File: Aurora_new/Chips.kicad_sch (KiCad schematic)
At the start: 84 parts, among them J1 UJ20-C-H-C-3-SMT-TR, J16 PPPC042LFBN-RC, J3 PPPC042LFBN-RC, J36 PPPC042LFBN-RC, J41 STEMMA QT, J6 DM3AT-SF-PEJM5, U1 STM32H757BITx, U13 XBP9X-DMUS-001, U14 MS5611-01BA, U2 USBLC6-2SC6, U3 TPS2121RUXR, U5 ICM-45686, U6 ICM-42688-P, U7 BNO085, U9 MCP23017T-E_SO

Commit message: bom updates (purchase links, prices, etc) and switching imu because out of stock
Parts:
- removed R12: 10k, Resistor_SMD:R_0805_2012Metric, symbol Device:R_Small
- removed U6: ICM-42688-P, ICM_42688_P:PQFN50P300X250X97-14N, symbol ICM-42688-P:ICM-42688-P
- added U6: ICM-40609-D, ICM-40609-D:XDCR_ICM-40609-D, symbol ICM-40609-D:ICM-40609-D
- C1, C10, C11, C12, C13, C14, C15, C16, C17, C18, C19, C2, C25, C27, C28, C3, C34, C36, C37, C38, C39, C4, C40, C46, C48, C5, C59, C6, C7, C8, C9: PURCHASE-URL (none) -> https://www.digikey.com/en/products/detail/kyocera-avx/KGM1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; Price (none) -> $0.00700
- C20, C26, C60: PURCHASE-URL (none) -> https://www.digikey.com/en/products/detail/samsung-electro-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; Price (none) -> $0.08000
- C21, C22, C23, C24: PURCHASE-URL (none) -> https://www.digikey.com/en/products/detail/samsung-electro-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; Price (none) -> $0.34380
- C29: footprint Capacitor_SMD:C_0805_2012Metric -> Capacitor_SMD:C_0201_0603Metric; PURCHASE-URL (none) -> https://www.digikey.com/en/products/detail/nextgen-componen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; Price (none) -> $0.08000
- C35, C41, C42: PURCHASE-URL (none) -> https://www.digikey.com/en/products/detail/nextgen-componen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; Price (none) -> $0.13880
- C43: value 100nF -> 0.1uF; footprint Capacitor_SMD:C_0805_2012Metric -> Capacitor_SMD:C_1206_3216Metric; PURCHASE-URL (none) -> https://www.digikey.com/en/products/detail/murata-electroni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; Price (none) -> $0.41890
- C44: value 10nF -> 2.2uF; footprint Capacitor_SMD:C_0805_2012Metric -> Capacitor_SMD:C_1206_3216Metric; PURCHASE-URL (none) -> https://www.digikey.com/en/products/detail/murata-electroni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; Price (none) -> $0.41890
- C45: value 2.2uF -> 10nF; footprint Capacitor_SMD:C_0805_2012Metric -> Capacitor_SMD:C_1206_3216Metric; PURCHASE-URL (none) -> https://www.digikey.com/en/products/detail/murata-electroni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; Price (none) -> $0.41890
- C49: PURCHASE-URL (none) -> https://www.digikey.com/en/products/detail/nextgen-componen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; Price (none) -> $0.17380
- C50: footprint Capacitor_SMD:C_0805_2012Metric -> Capacitor_SMD:C_1206_3216Metric; PURCHASE-URL (none) -> https://www.digikey.com/en/products/detail/murata-electroni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; Price (none) -> $0.41890
- D2: value LED -> BLUE LED; PURCHASE-URL (none) -> https://www.digikey.com/en/products/detail/w%C3%BCrth-elekt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; Price (none) -> $0.17600
- D3: value LED -> RED LED; PURCHASE-URL (none) -> https://www.digikey.com/en/products/detail/ams-osram-usa-in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; Price (none) -> $0.15000
- D4: value LED -> GREEN LED; PURCHASE-URL (none) -> https://www.digikey.com/en/products/detail/ams-osram-usa-in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; Price (none) -> $0.10200
- J1: PURCHASE-URL (none) -> https://www.digikey.com/en/products/detail/same-sky-formerl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; Price None -> $1.18000
- J16, J3, J36: PURCHASE-URL (none) -> https://www.digikey.com/en/products/detail/sullins-connecto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; Price (none) -> $0.59000
- J6: PURCHASE-URL (none) -> https://www.digikey.com/en/products/detail/hirose-electric-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; Price (none) -> $2.66000
- R1, R10, R11, R14, R18, R2, R21, R5, R7, R8, R9: PURCHASE-URL (none) -> https://www.digikey.com/en/products/detail/bourns-inc/CR080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; Price (none) -> $0.00442
- R13: value 10k -> 4.7kR; PURCHASE-URL (none) -> https://www.digikey.com/en/products/detail/bourns-inc/CR080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; Price (none) -> $0.00338
- R15: value 10k -> 620R; PURCHASE-URL (none) -> https://www.digikey.com/en/products/detail/bourns-inc/CR080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; Price (none) -> $0.00661
- R16: value 10k -> 1.3kR; PURCHASE-URL (none) -> https://www.digikey.com/en/products/detail/bourns-inc/CR080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; Price (none) -> $0.00661
- R3, R6: PURCHASE-URL (none) -> https://www.digikey.com/en/products/detail/bourns-inc/CR080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; Price (none) -> $0.00661
- R4: value 41k -> 41.2k; PURCHASE-URL (none) -> https://www.digikey.com/en/products/detail/bourns-inc/CR080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; Price (none) -> $0.00661
- U1: PURCHASE-URL (none) -> https://www.digikey.com/en/products/detail/stmicroelectroni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; Price (none) -> $19.24000
- U13: PURCHASE-URL (none) -> https://www.mouser.com/ProductDetail/Digi/XB9X-DMUS-001?qs=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; Price (none) -> $48.07
- U14: PURCHASE-URL (none) -> https://www.digikey.com/en/products/detail/te-connectivity-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; Price (none) -> $10.12000
- U2: PURCHASE-URL https://pricing.snapeda.com/search/part/USBLC6-2SC6/?ref=eda -> https://www.digikey.com/en/products/detail/stmicroelectroni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; Price (none) -> $0.36000
- U3: PURCHASE-URL (none) -> https://www.digikey.com/en/products/detail/texas-instrument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; Price (none) -> $2.37000
- U5: Price None -> (none)
- U7: PURCHASE-URL (none) -> https://www.digikey.com/en/products/detail/ceva-technologie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; Price None -> $13.05000
- U9: PURCHASE-URL (none) -> https://www.digikey.com/en/products/detail/microchip-techno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; Price (none) -> $1.62000
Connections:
- net 3V3_SENS: now also C44.2, C45.1, U6.13 (VDD), U6.8 (VDDIO); no longer C44.1, C45.2
- net GND: now also C44.1, C45.2, D2.1 (K), U6.11 (RESV), U6.18 (GND), U6.20 (RESV__1); no longer C44.2, C45.1
- net ICM456_CLK: no longer U1.58 (PA5)
- net ICM456_CS: no longer U1.85 (PE14)
- net ICM456_MISO: no longer U1.59 (PA6)
- net ICM456_MOSI: no longer U1.60 (PA7)
- net USB_VBUS: now also C27.1, J1.A4_B9 (VBUS), J1.A9_B4 (VBUS), R13.2, U2.5; no longer D2.1 (K)
- net ICM-406_INT1: now reaches U1.61 (PC4)
- net ICM-406_INT1: now also U6.12 (INT1/INT)
- net ICM-406_INT2: now reaches U1.62 (PC5)
- net ICM-406_INT2: now also U6.19 (INT2/FSYNC)
- net at D3.2 (A): now also R15.2; no longer R15.1
- net at U13.7 (DIO10/RSSI/PWM0): now also R15.1; no longer R15.2
- new net ICM406_CLK: U1.58 (PA5), U6.23 (SCL/SCLK)
- new net ICM406_CS: U1.85 (PE14), U6.22 (~{CS})
- new net ICM406_MISO: U1.59 (PA6), U6.9 (AD0/SDO)
- new net ICM406_MOSI: U1.60 (PA7), U6.24 (SDA/SDI/SDIO)
- no-connect marks 28 -> 22
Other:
- note added: "--ICM-40609-D-- Gyroscope Resistors/capacitors from datasheet (Fig 8)/Other designs SPI 3"
- note added: "GREEN LED"
- note added: "ICM-40609-D"
- note added: "RED LED"
- note removed: "--ICM-42688-- Gyroscope Resistors/capacitors from datasheet (Fig 7)/Other designs SPI 3"
- note removed: "<- BLUE LED"
- note removed: "AMBER LED"
- note removed: "ICM-42688-P"
- moved on the sheet: D2, R13

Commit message: undo imu switch grant got scammed
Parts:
- removed U6: ICM-40609-D, ICM-40609-D:XDCR_ICM-40609-D, symbol ICM-40609-D:ICM-40609-D
- added R12: 10k, Resistor_SMD:R_0805_2012Metric, symbol Device:R_Small
- added U6: ICM-42688-P, ICM-42688-P:PQFN50P300X250X97-14N, symbol ICM-42688-P:ICM-42688-P
- C43: value 0.1uF -> 100nF; footprint Capacitor_SMD:C_1206_3216Metric -> Capacitor_SMD:C_0805_2012Metric; PURCHASE-URL https://www.digikey.com/en/products/detail/murata-electroni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 -> https://www.digikey.com/en/products/detail/kyocera-avx/KGM1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; Price $0.41890 -> $0.00700
- C44, C45: footprint Capacitor_SMD:C_1206_3216Metric -> Capacitor_SMD:C_0805_2012Metric; PURCHASE-URL https://www.digikey.com/en/products/detail/murata-electroni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 -> https://www.digikey.com/en/products/detail/kyocera-avx/KGM1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; Price $0.41890 -> $0.00700
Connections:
- net ICM406_CLK is gone; now on net ICM426_CLK: U1.58 (PA5)
- net ICM406_MISO is gone; now on net ICM426_MISO: U1.59 (PA6)
- net ICM406_MOSI is gone; now on net ICM426_MOSI: U1.60 (PA7)
- net 3V3_SENS: now also R12.1, U6.5 (VDDIO), U6.8 (VDD)
- net GND: now also U6.6 (GND)
- net ICM426_CLK: now also U6.13 (AP_SCL/AP_SCLK)
- net ICM426_CS: now also R12.2, U6.12 (AP_CS)
- net ICM426_MISO: now also U6.1 (AP_SDO/AP_AD0)
- net ICM426_MOSI: now also U6.14 (AP_SDA/AP_SDIO/AP_SDI)
- net ICM-406_INT1 renamed ICM426_INT1
- net ICM426_INT1: now also U6.4 (INT1/INT)
- net ICM-406_INT2 renamed ICM426_INT2
- net ICM426_INT2: now also U6.9 (INT2/FSYNC/CLKIN)
- no-connect marks 22 -> 27
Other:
- note added: "--ICM-40609-D-- Gyroscope Resistors/capacitors from datasheet (Fig 7)/Other designs SPI 3"
- note added: "ICM-42688-P"
- note removed: "--ICM-40609-D-- Gyroscope Resistors/capacitors from datasheet (Fig 8)/Other designs SPI 3"
- note removed: "ICM-40609-D"

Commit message: added pyros, voltage booster
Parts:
- C29: footprint Capacitor_SMD:C_0201_0603Metric -> Capacitor_SMD:C_0805_2012Metric
- U13: PURCHASE-URL https://www.mouser.com/ProductDetail/Digi/XB9X-DMUS-001?qs=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 -> https://www.digikey.com/en/products/detail/digi/XB9X-DMUS-0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
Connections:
- net ADC2_SCL renamed TEMP_SCL
- net ADC2_SDA renamed TEMP_SDA
- net HDR_GPIO1 renamed PYRO1_CONT
- net HDR_GPIO2 renamed PYRO2_CONT
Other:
- moved on the sheet: J16, J3, J36

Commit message: working though GPIOs/CSs, Xref with cubeMX
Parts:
- removed R12: 10k, Resistor_SMD:R_0805_2012Metric, symbol Device:R_Small
- added R35: 10k, Resistor_SMD:R_0805_2012Metric, symbol Device:R_Small
- R11: value 10k -> 620R; PURCHASE-URL https://www.digikey.com/en/products/detail/bourns-inc/CR0805-FX-1002ELF/3593209 -> https://www.digikey.com/en/products/detail/bourns-inc/CR0805-FX-6200ELF/3785055; Price $0.00442 -> $0.00661
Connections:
- net UART5_RX is gone; now on net SLN_1: U1.101 (PB12)
- net UART5_TX is gone; now on net HDR_GPIO2: U1.102 (PB13)
- net 3V3: no longer C36.1, U5.5 (VDDIO)
- net 3V3_SENS: now also C36.1, U5.5 (VDDIO), U9.9 (VDD), R35.1; no longer R11.1
- net 3V3_XB: now also R11.1
- net 5V: no longer U9.9 (VDD)
- net GND: now also U5.12 (AP_CS), U6.12 (AP_CS), U9.15 (A0), U9.16 (A1), U9.17 (A2)
- net HDR_GPIO3: now also J36.4, U1.111 (PD12); no longer J36.3, U1.134 (PG4)
- net ICM426_CLK: no longer U1.58 (PA5)
- net ICM426_MISO: no longer U1.59 (PA6)
- net ICM426_MOSI: no longer U1.60 (PA7)
- net ICM456_CLK: now also U1.182 (PG11)
- net ICM456_INT: now also U1.67 (PF11)
- net ICM456_MISO: now also U1.180 (PG9)
- net ICM456_MOSI: now also U1.177 (PD7)
- net MISC_GPIO1: now also U1.27 (PF5); no longer U1.146 (PA8)
- net MISC_GPIO2: now also U1.26 (PF4); no longer U1.147 (PA9)
- net MISC_GPIO3: now also U1.25 (PF3); no longer U1.148 (PA10)
- net MISC_GPIO4: now also U1.24 (PF2); no longer U1.151 (PA13)
- net PYRO1_CONT: now also U1.104 (PB15); no longer U1.130 (PG2)
- net PYRO1_GPIO: now also U1.115 (PD14); no longer U1.176 (PD6)
- net PYRO2_CONT: now also U1.112 (PD13); no longer U1.131 (PG3)
- net PYRO2_GPIO: now also U1.116 (PD15); no longer U1.177 (PD7)
- net SERVO1: now also U1.138 (PG8); no longer U1.105 (PD8)
- net SERVO2: now also U1.137 (PG7); no longer U1.106 (PD9)
- net SERVO3: now also U1.136 (PG6); no longer U1.107 (PD10)
- net SERVO4: now also U1.135 (PG5); no longer U1.110 (PD11)
- net SERVO5: now also U1.134 (PG4); no longer U1.111 (PD12)
- net SERVO6: now also U1.131 (PG3); no longer U1.112 (PD13)
- net SERVO7: now also U1.130 (PG2); no longer U1.115 (PD14)
- net SLN_1: no longer U1.138 (PG8)
- net SLN_2: now also U1.107 (PD10); no longer U1.180 (PG9)
- net SPI6_CLK: now also U1.58 (PA5); no longer U1.184 (PG13)
- net SPI6_MISO: no longer U1.32 (PF8)
- net SPKG: now also U1.110 (PD11); no longer U1.137 (PG7)
- net XBP_CS: now also R11.2
- net HDR_GPIO1: now reaches U1.103 (PB14)
- net HDR_GPIO1: now also J36.3
- net DEBUG_SWCLK: now reaches U1.165 (PA14)
- net MCP230_INT1: now reaches U1.63 (PB0)
- net MCP230_INT1: now also U9.19 (INTB)
- net MCP230_INT2: now reaches U1.64 (PB1)
- net MCP230_INT2: now also U9.20 (INTA)
- net MCP_RESET: now reaches U1.66 (PI15)
- net MCP_RESET: now also U9.18 (~{RESET}), R35.2
- removed net HDR_GPIO4: J36.4, U1.135 (PG5)
- net HDR_GPIO5 renamed HDR_GPIO2
- net HDR_GPIO2: no longer U1.136 (PG6)
- net ICM426_CS: no longer names the net of U1.83 (PE12)
- net ICM426_CS: no longer U6.12 (AP_CS)
- removed net ICM456_CS: R11.2, U5.12 (AP_CS)
- new net DEBUG_SWDIO: U1.151 (PA13)
- new net SPI5_MISO: U1.32 (PF8)
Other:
- note added: "I2C address = 0x20"
- note removed: "RED LED"

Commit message: continued updating gpios and interrupt pins
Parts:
- added J50: PCB.RPSMAFRA.HT, KiCad(1):PCBRPSMAFRAHT, symbol PCB_RPSMAFRA_HT:PCB.RPSMAFRA.HT
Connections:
- net B/R_CLK: now also U13.14 (DO18/SPI_CLK); no longer U13.31 (DIO2/AD2)
- net GND: now also U5.10 (RESV/AUX1_CS), U5.11 (RESV/AUX1_SDO), U5.2 (RESV/AUX1_SDIO/AUX1_SDI/MAS_DA), U5.3 (RESV/AUX1_SCLK/MAS_CLK), U5.7 (RESV), U6.10 (RESV_10), U6.11 (RESV_11), U6.2 (RESV_2), U6.3 (RESV_3), U6.7 (RESV_7), J50.2, J50.3, J50.4, J50.5
- net ICM426_INT2: now also U1.83 (PE12); no longer U1.62 (PC5)
- net XBP_CS: now also U13.15 (DO17/~{SPI_SSEL}); no longer U13.30 (DIO3/AD3)
- net ICM456_INT2: now reaches U5.9 (INT2/FSYNC/CLKIN)
- net ICM456_INT2: now also U1.78 (PE9)
- net XB_RESET: now reaches U1.3 (PE4)
- net XB_RESET: now also U13.6 (~{RESET})
- net XB_INT: now reaches U1.75 (PG1)
- net XB_INT: now also U13.12 (DO19/~{SPI_ATTN})
- net XBP_ATTN renamed XBP_ANTENNA
- net XBP_ANTENNA: now also J50.1
- net XB_RX: no longer names the net of U1.45 (PA0)
- net XB_RX: no longer U13.4 (DIO14/DIN/~{CONFIG})
- net XB_TX: no longer names the net of U1.13 (PI9)
- net XB_TX: no longer U13.3 (DIO13/DOUT)
- no-connect marks 27 -> 16
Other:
- note added: "Antenna Connector"
- note removed: "*"
- moved on the sheet: R11

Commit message: BNO/baro pins, pullups added to all active low pins on Baro
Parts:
- added R12, R36: 10k, Resistor_SMD:R_0805_2012Metric, symbol Device:R_Small
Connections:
- net STM_INTN is gone; now on net BNO_INT: U7.14 (~{H_INT})
- net 3V3: now also R12.1, R36.2; no longer U7.5 (PS1)
- net 3V3_SENS: now also U7.5 (PS1)
- net BARO_CS: now also U1.157 (PH14)
- net BNO_BOOTN: now also U1.163 (PI2)
- net BNO_CLKSEL0: now also R36.1
- net BNO_NRST: now also U1.162 (PI1), R12.2
- net BNO_WAKE/PS0: now also U1.159 (PI0)
- net STM_CSN: no longer U7.18 (~{H_CS})
- net BNO_CS: now reaches U1.158 (PH15)
- net BNO_CS: now also U7.18 (~{H_CS})
- net BNO_INT: now reaches U1.69 (PF13)
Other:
- moved on the sheet: D5

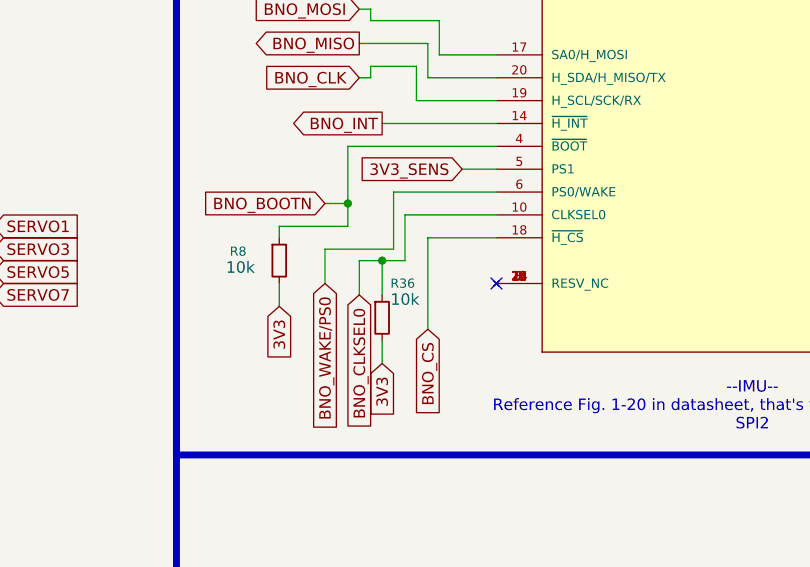
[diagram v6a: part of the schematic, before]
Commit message: pullup on BNO CS
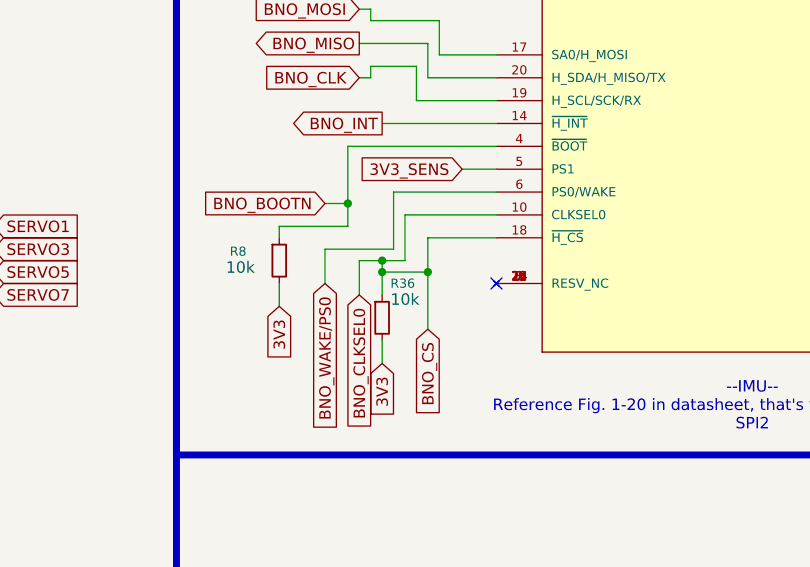
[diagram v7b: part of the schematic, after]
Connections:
- net BNO_CS is gone; now on net BNO_CLKSEL0: U1.158 (PH15), U7.18 (~{H_CS})
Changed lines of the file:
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@@
 	)
 	(junction
+		(at 482.6 355.6)
+		(diameter 0)
+		(color 0 0 0 0)
+	)
+	(junction
 		(at 532.13 86.36)
 		(diameter 0)
@@
 	)
 	(junction
+		(at 487.68 355.6)
+		(diameter 0)
+		(color 0 0 0 0)
+	)
+	(junction
 		(at 275.59 365.76)
 		(diameter 0)
@@
 	(wire
 		(pts
+			(xy 487.68 355.6) (xy 487.68 361.95)
+		)
+		(stroke
+			(width 0)
+			(type default)
+		)
+	)
+	(wire
+		(pts
 			(xy 43.18 57.15) (xy 45.72 57.15)
 		)
@@
 	(wire
 		(pts
+			(xy 482.6 355.6) (xy 487.68 355.6)
+		)
+		(stroke
+			(width 0)
+			(type default)
+		)
+	)
+	(wire
+		(pts
 			(xy 443.23 140.97) (xy 447.04 140.97)
 		)
@@
 	(wire
 		(pts
+			(xy 482.6 355.6) (xy 482.6 358.14)
+		)
+		(stroke
+			(width 0)
+			(type default)
+		)
+	)
+	(wire
+		(pts
 			(xy 363.22 246.38) (xy 363.22 247.65)
 		)
@@
 	(wire
 		(pts
-			(xy 482.6 354.33) (xy 482.6 358.14)
+			(xy 482.6 354.33) (xy 482.6 355.6)
 		)
 		(stroke
@@
 	(wire
 		(pts
-			(xy 487.68 351.79) (xy 487.68 361.95)
+			(xy 487.68 351.79) (xy 487.68 355.6)
 		)
 		(stroke

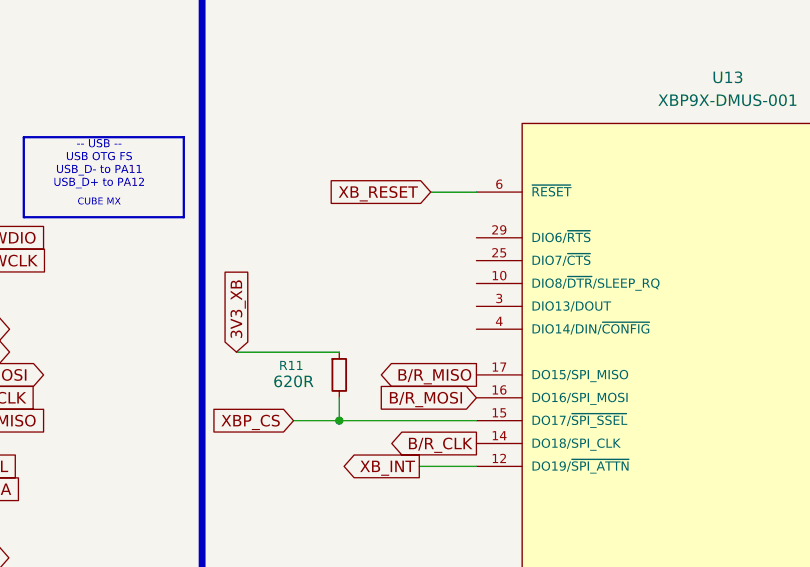
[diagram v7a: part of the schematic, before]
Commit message: done with debug header pins
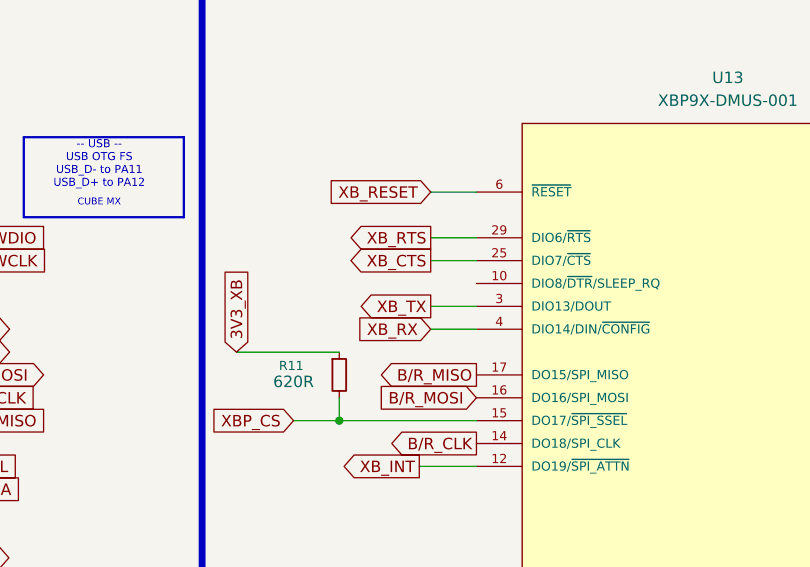
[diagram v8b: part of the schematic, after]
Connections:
- net XB_CTS: now reaches U13.25 (DIO7/~{CTS})
- net XB_RTS: now reaches U13.29 (DIO6/~{RTS})
- net XB_TX: now reaches U13.3 (DIO13/DOUT)
- net XB_RX: now reaches U13.4 (DIO14/DIN/~{CONFIG})
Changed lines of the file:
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@@
 	(wire
 		(pts
+			(xy 241.3 158.75) (xy 246.38 158.75)
+		)
+		(stroke
+			(width 0)
+			(type default)
+		)
+	)
+	(wire
+		(pts
 			(xy 182.88 143.51) (xy 180.34 143.51)
 		)
@@
 	(wire
 		(pts
+			(xy 241.3 148.59) (xy 246.38 148.59)
+		)
+		(stroke
+			(width 0)
+			(type default)
+		)
+	)
+	(wire
+		(pts
 			(xy 499.11 71.12) (xy 501.65 71.12)
 		)
@@
 	(wire
 		(pts
+			(xy 241.3 151.13) (xy 246.38 151.13)
+		)
+		(stroke
+			(width 0)
+			(type default)
+		)
+	)
+	(wire
+		(pts
 			(xy 50.8 87.63) (xy 50.8 88.9)
 		)
@@
 	(wire
 		(pts
+			(xy 241.3 156.21) (xy 246.38 156.21)
+		)
+		(stroke
+			(width 0)
+			(type default)
+		)
+	)
+	(wire
+		(pts
 			(xy 106.68 48.26) (xy 113.03 48.26)
 		)
@@
 		)
 	)
+	(global_label "XB_RTS"
+		(shape output)
+		(at 241.3 148.59 180)
+		(fields_autoplaced yes)
+		(effects
+			(font
+				(size 1.27 1.27)
+			)
+			(justify right)
+		)
+		(property "Intersheetrefs" "${INTERSHEET_REFS}"
+			(at 231.4206 148.59 0)
+			(effects
+				(font
+					(size 1.27 1.27)
+				)
+				(justify right)
+				(hide yes)
+			)
+		)
+	)
 	(global_label "SLN_2"
 		(shape output)
@@
 		)
 	)
+	(global_label "XB_TX"
+		(shape output)
+		(at 241.3 156.21 180)
+		(fields_autoplaced yes)
+		(effects
+			(font
+				(size 1.27 1.27)
+			)
+			(justify right)
+		)
+		(property "Intersheetrefs" "${INTERSHEET_REFS}"
+			(at 232.6906 156.21 0)
+			(effects
+				(font
+					(size 1.27 1.27)
+				)
+				(justify right)
+				(hide yes)
+			)
+		)
+	)
 	(global_label "BNO_MISO"
 		(shape input)
@@
 		)
 	)
+	(global_label "XB_RX"
+		(shape input)
+		(at 241.3 158.75 180)
+		(fields_autoplaced yes)
+		(effects
+			(font
+				(size 1.27 1.27)
+			)
+			(justify right)
+		)
+		(property "Intersheetrefs" "${INTERSHEET_REFS}"
+			(at 232.3882 158.75 0)
+			(effects
+				(font
+					(size 1.27 1.27)
+				)
+				(justify right)
+				(hide yes)
+			)
+		)
+	)
 	(global_label "SD_CLK"
 		(shape input)
@@
 				(hide yes)
 			)
+		)
+	)
+	(global_label "XB_CTS"
+		(shape output)
+		(at 241.3 151.13 180)
+		(fields_autoplaced yes)
+		(effects
+			(font
+				(size 1.27 1.27)
+			)
+			(justify right)
+		)
+		(property "Intersheetrefs" "${INTERSHEET_REFS}"
+			(at 231.4206 151.13 0)
+			(effects
+				(font
+					(size 1.27 1.27)
+				)
+				(justify right)
+				(hide yes)
+			)
